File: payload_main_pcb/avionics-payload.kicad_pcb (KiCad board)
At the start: 2 copper layers, 80 x 80 mm, 25 parts, among them J1 Conn_Coaxial_x2, SW1 SW_Push, SW2 SW_Push, U1 ADXL357BEZ, U2 Teensy4.0, U3 RFM96W-433S2, U4 ublox_SAM-M8Q, U5 MS5607-02BA

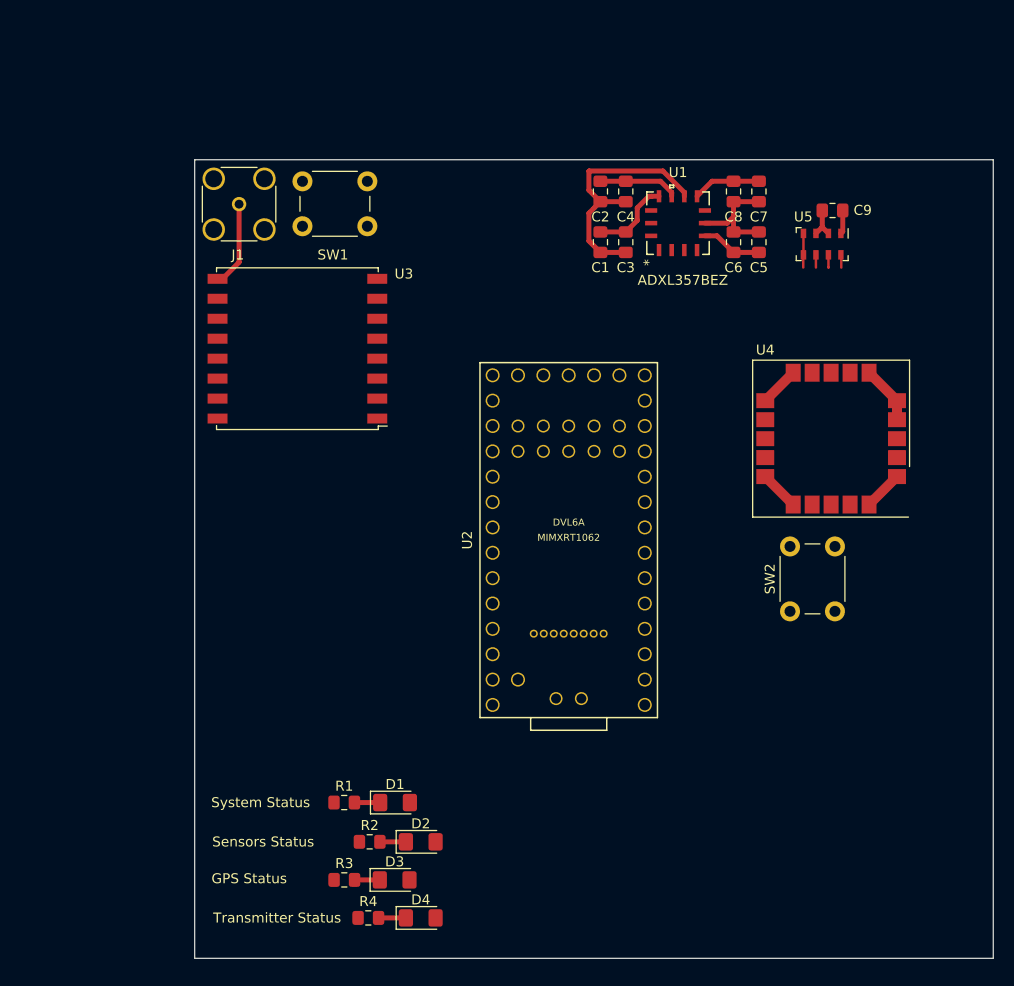
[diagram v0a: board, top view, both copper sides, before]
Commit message: Work on ground station and new IMU added to payload
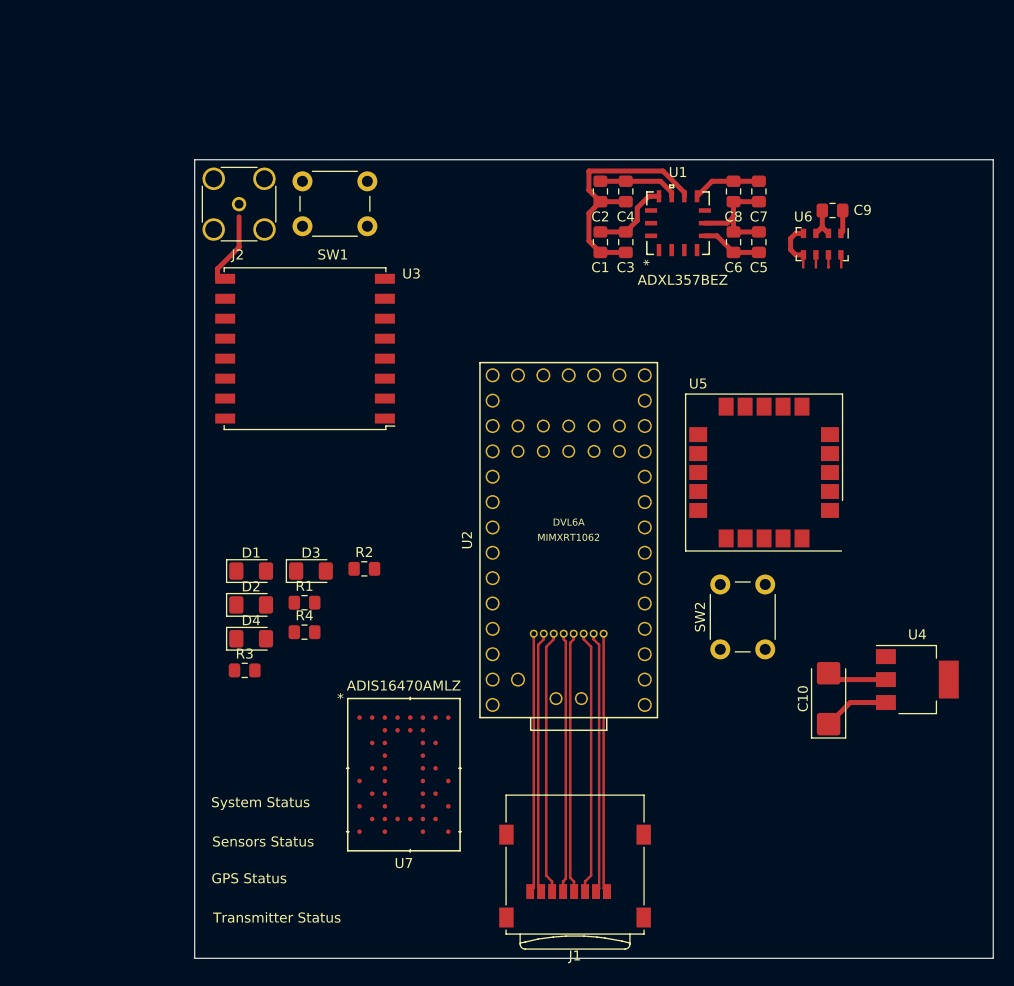
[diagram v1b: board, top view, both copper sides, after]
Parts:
- added C10: CP1, Capacitor_Tantalum_SMD:CP_EIA-6032-15_Kemet-U_Pad2.25x2.35mm_HandSolder, F.Cu at (103.5, 94.0)
- added J1: Micro_SD_Card, Connector_Card:microSD_HC_Wuerth_693072010801, F.Cu at (78.1, 111.8)
- added U4: LT1129-3.3_SOT223, Package_TO_SOT_SMD:SOT-223-3_TabPin2, F.Cu at (112.4, 92.1)
- added U7: ADIS16470AMLZ, footprints:ADIS16470AMLZ, F.Cu at (61.0, 101.6)
- moved D4 32.7 mm to (45.7, 88.0)
- moved D3 32.1 mm to (51.7, 81.2)
- moved R4 29.3 mm to (51.0, 87.3), turned to 0 degrees
- moved D2 29.2 mm to (45.7, 84.6)
- moved R2 27.4 mm to (57.0, 81.0)
- moved D1 27.3 mm to (45.7, 81.2)
- moved R3 23.2 mm to (45.0, 91.2)
- moved R1 20.4 mm to (51.0, 84.4)
- moved SW2 7.96 mm to (92.7, 89.0)
- moved U5 7.52 mm to (97.0, 71.3)
- moved U3 0.76 mm to (51.1, 58.9)
- renumbered J1 to J2, U4 to U5, U5 to U6
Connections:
- D1 pad 2: Net-(D1-Pad2) -> SystemStatus
- D2 pad 2: Net-(D2-Pad2) -> SensorStatus
- D3 pad 2: Net-(D3-Pad2) -> TransmitterStatus
- D4 pad 2: Net-(D4-Pad2) -> GPSStatus
- R4 pad 1: Net-(D4-Pad1) -> GND
- R4 pad 2: GND -> Net-(D4-Pad1)
- U2 pad 2: Net-(U2-Pad2) -> MISO2
- U2 pad 27: Net-(D1-Pad2) -> Net-(U2-Pad27)
- U2 pad 28: Net-(D2-Pad2) -> Net-(U2-Pad28)
- U2 pad 29: Net-(D3-Pad2) -> Net-(U2-Pad29)
- U2 pad 3: Net-(U2-Pad3) -> CS2
- U2 pad 30: Net-(D4-Pad2) -> Net-(U2-Pad30)
- U2 pad 37: Net-(U2-Pad37) -> MOSI2
- U2 pad 38: Net-(U2-Pad38) -> SCK2
- U2 pad 4: Net-(U2-Pad4) -> GPSStatus
- U2 pad 45: MISO2 -> SD_DAT1
- U2 pad 46: MOSI2 -> SD_DAT0
- U2 pad 47: GND -> SD_GND
- U2 pad 48: CS2 -> SD_CLK
- U2 pad 49: +3V3 -> SD_3.3
- U2 pad 5: Net-(U2-Pad5) -> SensorStatus
- U2 pad 50: SCK2 -> SD_CMD
- U2 pad 51: Net-(U2-Pad51) -> SD_DAT3
- U2 pad 52: Net-(U2-Pad52) -> SD_DAT2
- U2 pad 6: Net-(U2-Pad6) -> TransmitterStatus
- U2 pad 7: Net-(U2-Pad7) -> SystemStatus
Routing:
- net SD_CMD: track 0.00 -> 26.4 mm
- net SD_GND: track 0.00 -> 26.4 mm
- net SD_DAT3: track 0.00 -> 26.2 mm
- net SD_DAT0: track 0.00 -> 26.2 mm
- net SD_3.3: track 0.00 -> 26.1 mm
- net SD_CLK: track 0.00 -> 26.0 mm
- net SD_DAT1: track 0.00 -> 26.0 mm
- net SD_DAT2: track 0.00 -> 26.0 mm
- net GND: track 57.9 -> 46.2 mm
- net +3V3: track 16.6 -> 23.2 mm
- net Net-(D4-Pad1): track 2.74 -> 0.00 mm
- net Net-(D2-Pad1): track 2.60 -> 0.00 mm
- net Net-(D1-Pad1): track 2.58 -> 0.00 mm
- net Net-(D3-Pad1): track 2.53 -> 0.00 mm
- net CS1:1: track 3.43 -> 5.40 mm
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
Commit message: Added logo to board
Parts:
- added Ref**: Val**, footprints:drawing, F.Cu at (69.8, 75.6)
- moved C10 36.4 mm to (113.7, 59.1)
- moved U4 20.3 mm to (112.4, 71.8)
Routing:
- net +3V3: track 23.2 -> 16.6 mm
- net GND: track 46.2 -> 40.2 mm

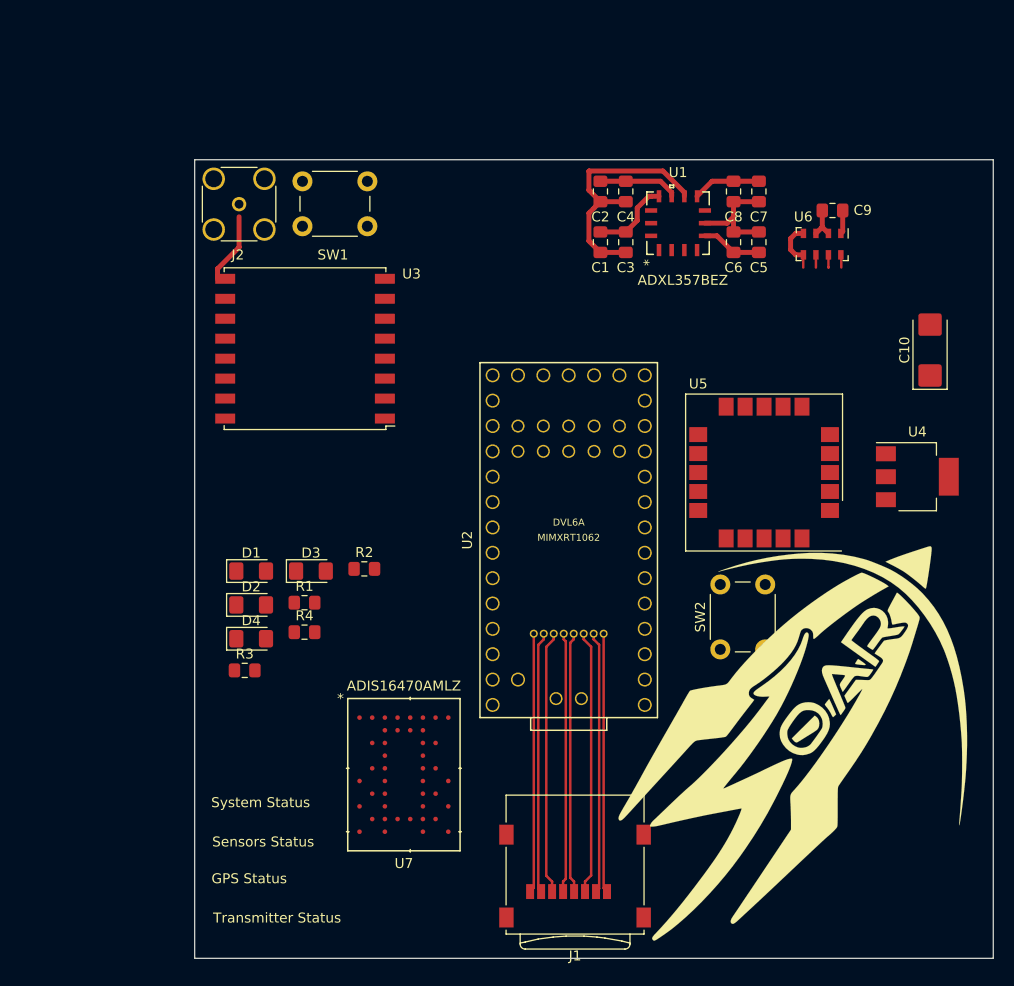
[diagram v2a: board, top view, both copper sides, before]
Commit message: Wired boards using autorouter
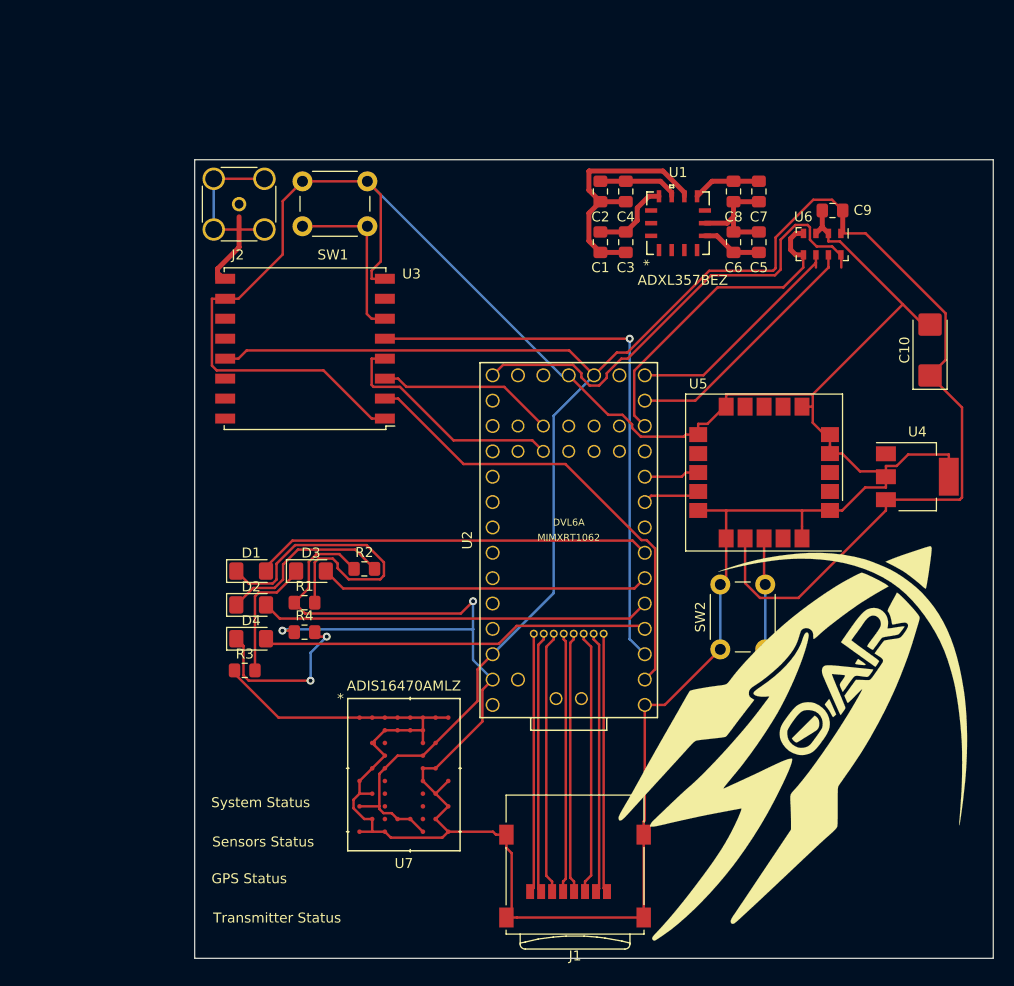
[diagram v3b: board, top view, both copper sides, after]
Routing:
- net GND: track 40.2 -> 444.9 mm, vias 0 -> 2
- net +3V3: track 16.6 -> 216.3 mm
- net CS2: track 0.00 -> 56.8 mm, vias 0 -> 1
- net SCK1: track 1.29 -> 48.5 mm
- net MISO2: track 0.00 -> 46.8 mm
- net SystemStatus: track 0.00 -> 40.0 mm
- net SensorStatus: track 0.00 -> 39.1 mm
- net GPSStatus: track 0.00 -> 39.0 mm
- net TransmitterStatus: track 0.00 -> 33.1 mm
- net Net-(D1-Pad1): track 0.00 -> 32.3 mm
- net CS1:1: track 5.40 -> 32.6 mm
- net MOSI1: track 1.28 -> 25.2 mm
- net SCK2: track 0.00 -> 23.9 mm
- net MISO1: track 1.27 -> 23.1 mm
- net MOSI2: track 0.00 -> 17.8 mm
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
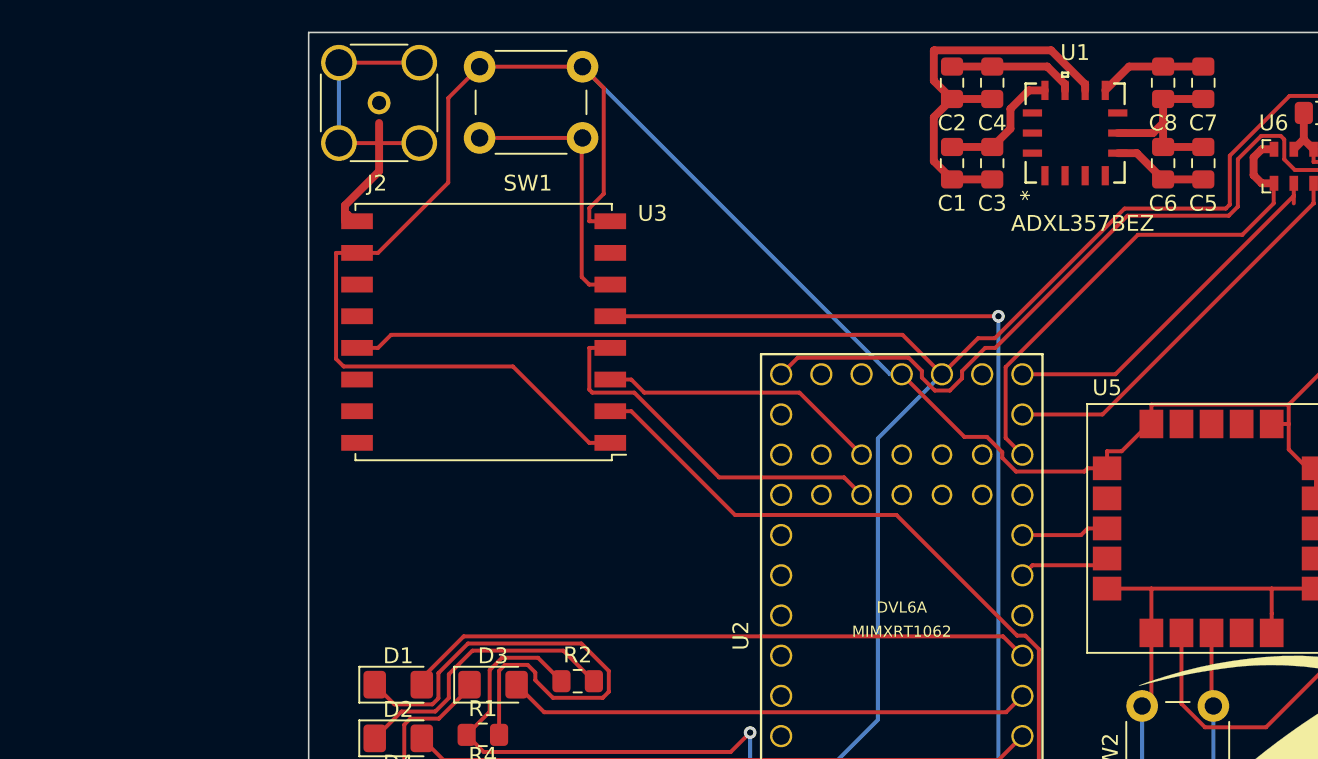
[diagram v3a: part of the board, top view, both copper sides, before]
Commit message: Integrated ADIS16470 in schematic and removed ADXL357
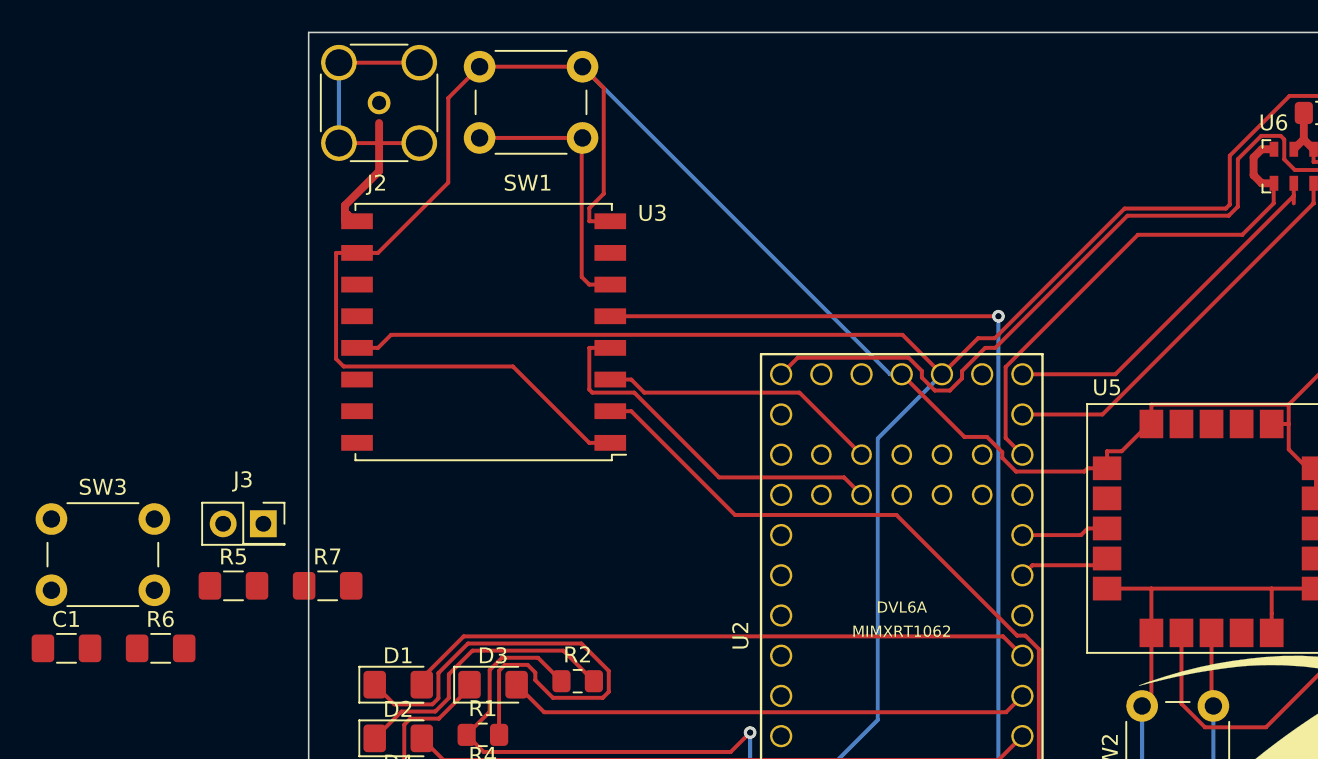
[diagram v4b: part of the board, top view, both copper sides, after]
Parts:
- removed C2, C5, C7: 1uF, Capacitor_SMD:C_0805_2012Metric_Pad1.15x1.40mm_HandSolder
- removed C3, C4, C6, C8: .1uF, Capacitor_SMD:C_0805_2012Metric_Pad1.15x1.40mm_HandSolder
- removed U1: ADXL357BEZ, footprints:ADXL357BEZ
- added J3: Screw_Terminal_01x02, Connector_PinSocket_2.54mm:PinSocket_2x01_P2.54mm_Vertical, F.Cu at (37.1, 71.0)
- added R5: 10k, Resistor_SMD:R_1206_3216Metric_Pad1.42x1.75mm_HandSolder, F.Cu at (35.3, 75.0)
- added R6: 10k, Resistor_SMD:R_1206_3216Metric_Pad1.42x1.75mm_HandSolder, F.Cu at (30.7, 78.9)
- added R7: 10k, Resistor_SMD:R_1206_3216Metric_Pad1.42x1.75mm_HandSolder, F.Cu at (41.2, 75.0)
- added SW3: SW_Push, Button_Switch_THT:SW_PUSH_6mm, F.Cu at (23.8, 70.7)
- C1: value 1uF -> 100nF; footprint Capacitor_SMD:C_0805_2012Metric_Pad1.15x1.40mm_HandSolder -> Capacitor_SMD:C_1206_3216Metric_Pad1.42x1.75mm_HandSolder
- C10: value CP1 -> 3.3uF
- moved C1 63.8 mm to (24.7, 78.9), turned to 0 degrees
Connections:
- U2 pad 28: Net-(U2-Pad28) -> IMU_DR
- U7 pad G3: Net-(U7-PadG3) -> CS1:2
- U7 pad G6: Net-(U7-PadG6) -> MOSI1
- U7 pad H3: Net-(U7-PadH3) -> MISO1
- U7 pad H6: Net-(U7-PadH6) -> SCK1
- U7 pad J6: Net-(U7-PadJ6) -> IMU_DR
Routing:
- net GND: track 444.9 -> 408.1 mm
- net +3V3: track 216.3 -> 202.1 mm
- net Net-(C2-Pad1): track 7.99 -> 0.00 mm
- net Net-(C7-Pad1): track 6.82 -> 0.00 mm
